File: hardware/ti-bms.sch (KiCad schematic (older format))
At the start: 43 parts, among them J1 Conn_02x04_Odd_Even, J2 Conn_02x03_Odd_Even, J4 CAN_TERM, U1 Pico, U2 MCP2515-xST, U3 SN65HVD230, U4 TPS62160DGK, U5 MAX3485, U6 MAX3485

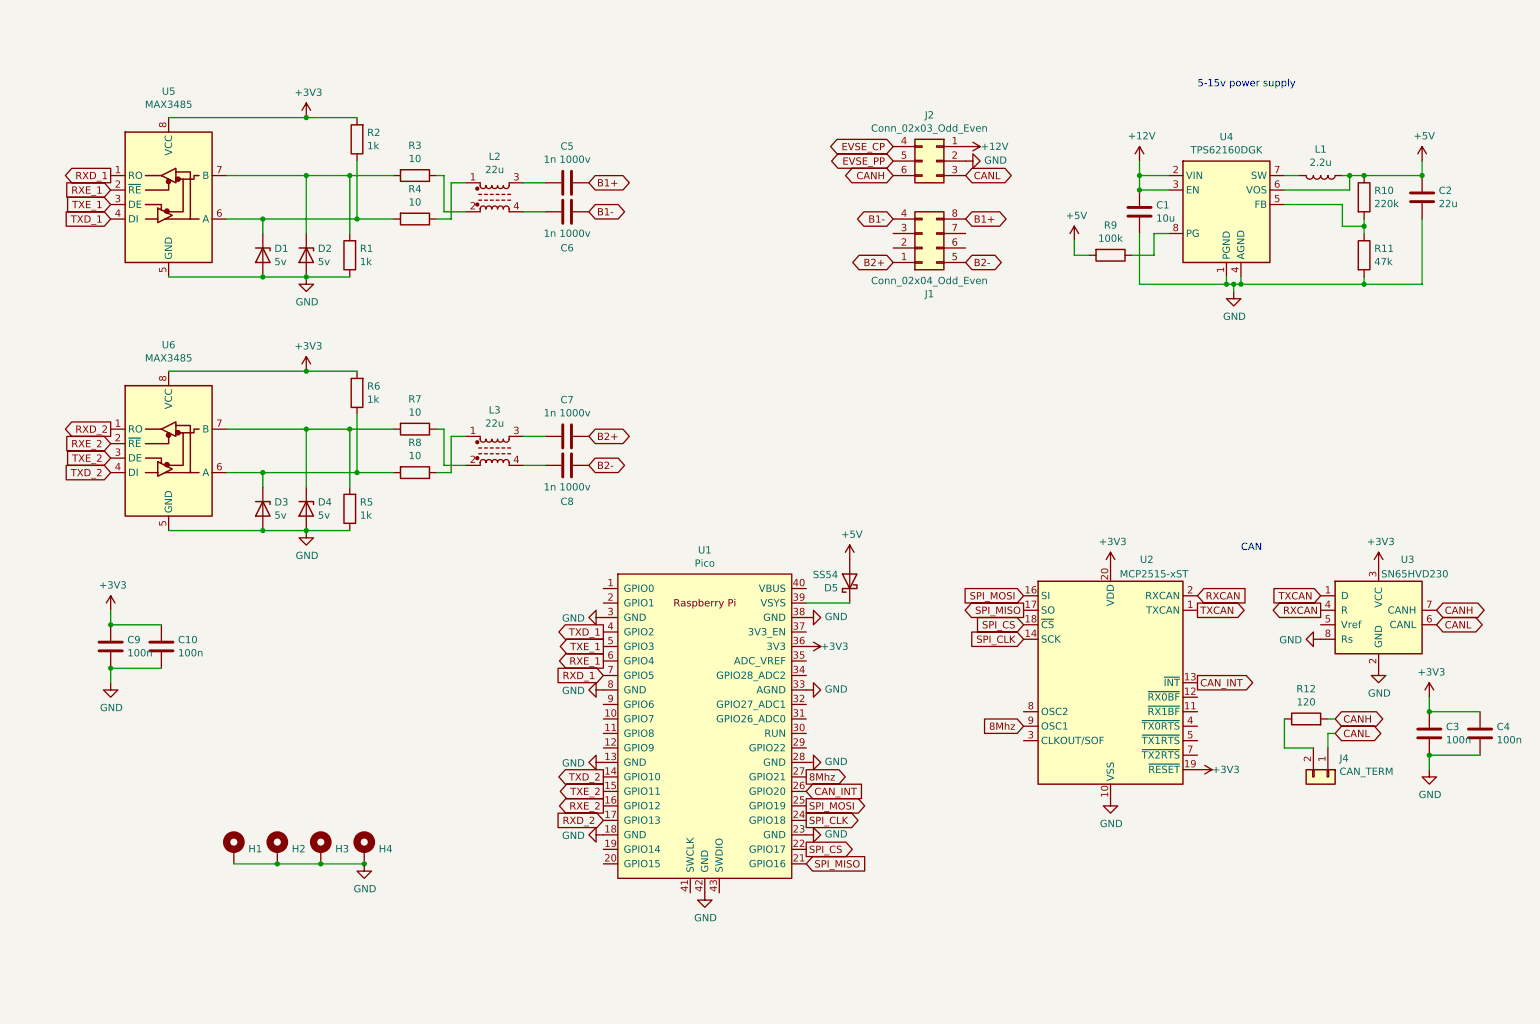
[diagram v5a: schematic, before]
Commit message: add 12v input and output, connect CAN line driver sleep pin
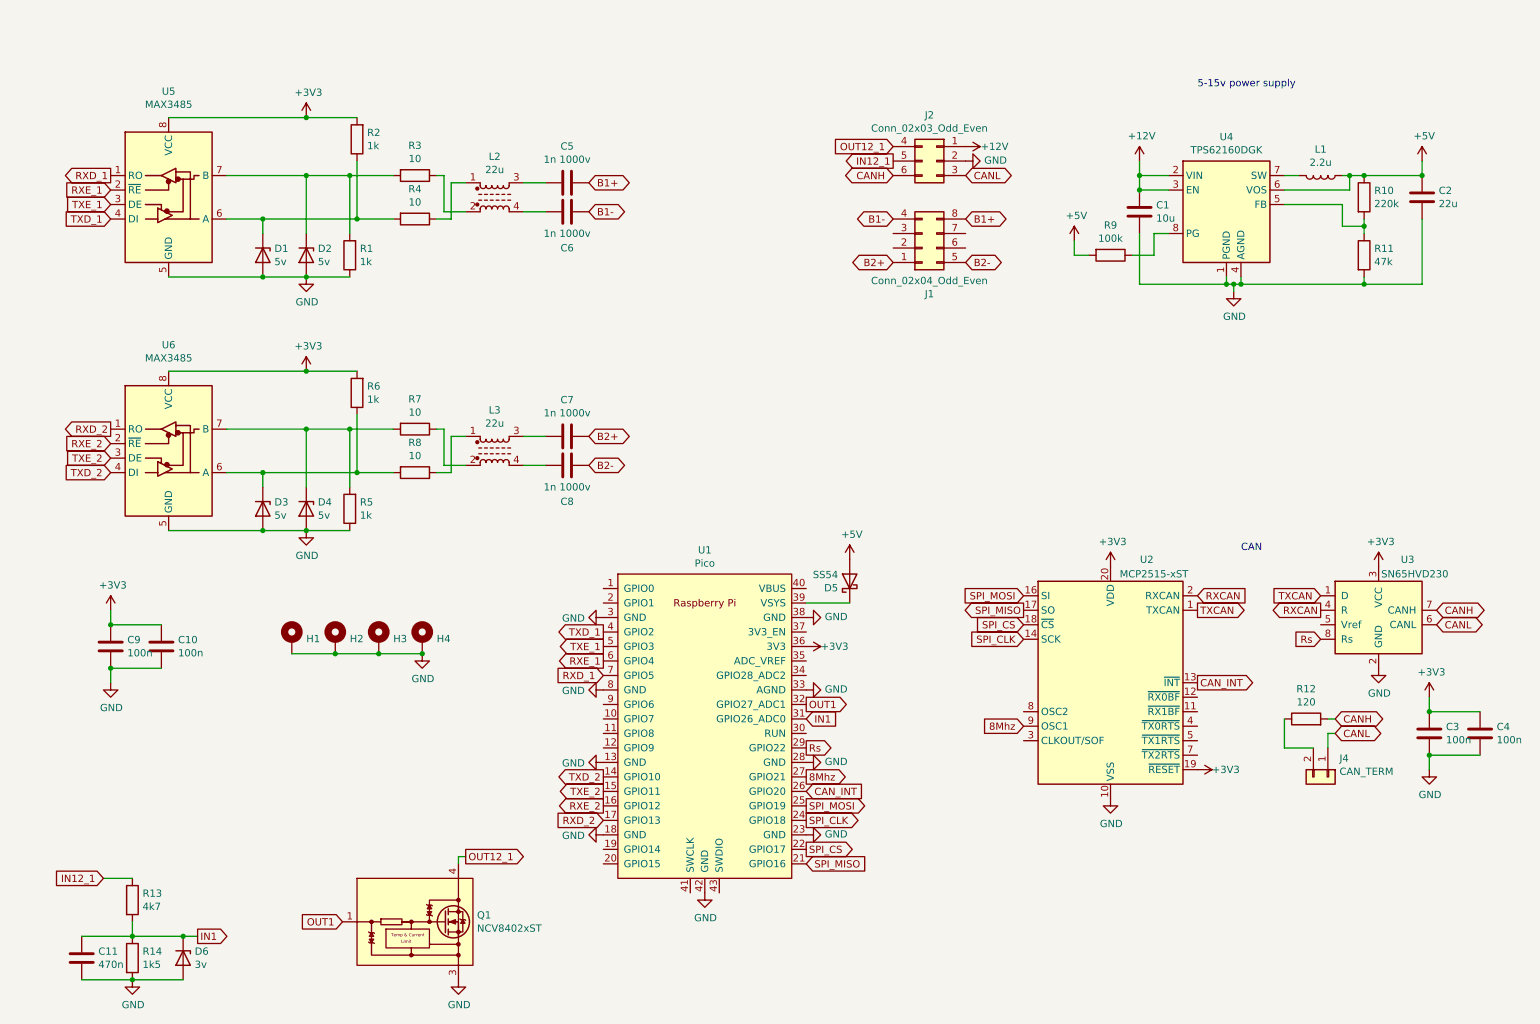
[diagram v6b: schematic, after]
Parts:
- added C11: 470n, Capacitor_SMD:C_0603_1608Metric, symbol Device:C
- added D6: 3v, Diode_SMD:D_MiniMELF, symbol Device:D_Zener
- added Q1: NCV8402xST, Package_TO_SOT_SMD:SOT-223, symbol Driver_FET:NCV8402xST
- added R13: 4k7, Resistor_SMD:R_0603_1608Metric, symbol Device:R
- added R14: 1k5, Resistor_SMD:R_0603_1608Metric, symbol Device:R
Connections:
- net GND: now also C11.2, D6.2 (A), Q1.3 (S), R14.2; no longer U3.8 (Rs)
- net Rs: now reaches U1.29 (GPIO22)
- net Rs: now also U3.8 (Rs)
- net IN1: now reaches U1.31 (GPIO26_ADC0)
- net IN1: now also C11.1, D6.1 (K), R13.2, R14.1
- net OUT1: now reaches U1.32 (GPIO27_ADC1)
- net OUT1: now also Q1.1 (G)
- net EVSE_CP renamed OUT12_1
- net OUT12_1: now also Q1.2 (D), Q1.4 (D)
- net EVSE_PP renamed IN12_1
- net IN12_1: now also R13.1
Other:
- moved on the sheet: H1, H2, H3, H4
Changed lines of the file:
@@
-$EndComp
-$Comp
-L power:GND #PWR024
-U 1 1 617A7038
-P 9650 4900
-F 0 "#PWR024" H 9650 4650 50  0001 C CNN
-F 1 "GND" V 9655 4772 50  0000 R CNN
-F 2 "" H 9650 4900 50  0001 C CNN
-F 3 "" H 9650 4900 50  0001 C CNN
-	1    9650 4900
-	0    1    1    0
 $EndComp
 $Comp
@@
 L Mechanical:MountingHole_Pad H1
 U 1 1 6199AFD3
-P 2150 6350
-F 0 "H1" H 2250 6353 50  0000 L CNN
-F 1 "MountingHole" H 2250 6308 50  0001 L CNN
-F 2 "MountingHole:MountingHole_3.2mm_M3_Pad" H 2150 6350 50  0001 C CNN
-F 3 "~" H 2150 6350 50  0001 C CNN
-	1    2150 6350
+P 2550 4900
+F 0 "H1" H 2650 4903 50  0000 L CNN
+F 1 "MountingHole" H 2650 4858 50  0001 L CNN
+F 2 "MountingHole:MountingHole_3.2mm_M3_Pad" H 2550 4900 50  0001 C CNN
+F 3 "~" H 2550 4900 50  0001 C CNN
+	1    2550 4900
 	1    0    0    -1
 $EndComp
@@
 L Mechanical:MountingHole_Pad H2
 U 1 1 6199C740
-P 2450 6350
-F 0 "H2" H 2550 6353 50  0000 L CNN
-F 1 "MountingHole" H 2550 6308 50  0001 L CNN
-F 2 "MountingHole:MountingHole_3.2mm_M3_Pad" H 2450 6350 50  0001 C CNN
-F 3 "~" H 2450 6350 50  0001 C CNN
-	1    2450 6350
+P 2850 4900
+F 0 "H2" H 2950 4903 50  0000 L CNN
+F 1 "MountingHole" H 2950 4858 50  0001 L CNN
+F 2 "MountingHole:MountingHole_3.2mm_M3_Pad" H 2850 4900 50  0001 C CNN
+F 3 "~" H 2850 4900 50  0001 C CNN
+	1    2850 4900
 	1    0    0    -1
 $EndComp
@@
 L Mechanical:MountingHole_Pad H3
 U 1 1 6199C8D6
-P 2750 6350
-F 0 "H3" H 2850 6353 50  0000 L CNN
-F 1 "MountingHole" H 2850 6305 50  0001 L CNN
-F 2 "MountingHole:MountingHole_3.2mm_M3_Pad" H 2750 6350 50  0001 C CNN
-F 3 "~" H 2750 6350 50  0001 C CNN
-	1    2750 6350
+P 3150 4900
+F 0 "H3" H 3250 4903 50  0000 L CNN
+F 1 "MountingHole" H 3250 4855 50  0001 L CNN
+F 2 "MountingHole:MountingHole_3.2mm_M3_Pad" H 3150 4900 50  0001 C CNN
+F 3 "~" H 3150 4900 50  0001 C CNN
+	1    3150 4900
 	1    0    0    -1
 $EndComp
@@
 L Mechanical:MountingHole_Pad H4
 U 1 1 6199CA74
-P 3050 6350
-F 0 "H4" H 3150 6353 50  0000 L CNN
-F 1 "MountingHole" H 3150 6305 50  0001 L CNN
-F 2 "MountingHole:MountingHole_3.2mm_M3_Pad" H 3050 6350 50  0001 C CNN
-F 3 "~" H 3050 6350 50  0001 C CNN
-	1    3050 6350
-	1    0    0    -1
-$EndComp
-Wire Wire Line
-	2150 6450 2450 6450
-Connection ~ 2450 6450
-Wire Wire Line
-	2450 6450 2750 6450
-Connection ~ 2750 6450
-Wire Wire Line
-	2750 6450 3050 6450
+P 3450 4900
+F 0 "H4" H 3550 4903 50  0000 L CNN
+F 1 "MountingHole" H 3550 4855 50  0001 L CNN
+F 2 "MountingHole:MountingHole_3.2mm_M3_Pad" H 3450 4900 50  0001 C CNN
+F 3 "~" H 3450 4900 50  0001 C CNN
+	1    3450 4900
+	1    0    0    -1
+$EndComp
+Wire Wire Line
+	2550 5000 2850 5000
+Connection ~ 2850 5000
+Wire Wire Line
+	2850 5000 3150 5000
+Connection ~ 3150 5000
+Wire Wire Line
+	3150 5000 3450 5000
 $Comp
 L power:GND #PWR031
 U 1 1 619B5460
-P 3050 6450
-F 0 "#PWR031" H 3050 6200 50  0001 C CNN
-F 1 "GND" H 3055 6277 50  0000 C CNN
-F 2 "" H 3050 6450 50  0001 C CNN
-F 3 "" H 3050 6450 50  0001 C CNN
-	1    3050 6450
-	1    0    0    -1
-$EndComp
-Connection ~ 3050 6450
+P 3450 5000
+F 0 "#PWR031" H 3450 4750 50  0001 C CNN
+F 1 "GND" H 3455 4827 50  0000 C CNN
+F 2 "" H 3450 5000 50  0001 C CNN
+F 3 "" H 3450 5000 50  0001 C CNN
+	1    3450 5000
+	1    0    0    -1
+$EndComp
+Connection ~ 3450 5000
 $Comp
 L Regulator_Switching:TPS62160DGK U4
@@
 	0    1    1    0
 $EndComp
-Text GLabel 6700 1500 0    50   BiDi ~ 0
-EVSE_CP
-Text GLabel 6700 1600 0    50   BiDi ~ 0
-EVSE_PP
 Text GLabel 7200 1700 2    50   BiDi ~ 0
 CANL
@@
 Wire Wire Line
 	1300 5100 1300 5200
+$Comp
+L Device:R R13
+U 1 1 61DD7F66
+P 1450 6700
+F 0 "R13" H 1520 6746 50  0000 L CNN
+F 1 "4k7" H 1520 6655 50  0000 L CNN
+F 2 "Resistor_SMD:R_0603_1608Metric" V 1380 6700 50  0001 C CNN
+F 3 "~" H 1450 6700 50  0001 C CNN
+F 4 "C23162" H 1450 6700 50  0001 C CNN "LCSC"
+	1    1450 6700
+	1    0    0    -1
+$EndComp
+$Comp
+L Device:R R14
+U 1 1 61DD8D2C
+P 1450 7100
+F 0 "R14" H 1520 7146 50  0000 L CNN
+F 1 "1k5" H 1520 7055 50  0000 L CNN
+F 2 "Resistor_SMD:R_0603_1608Metric" V 1380 7100 50  0001 C CNN
+F 3 "~" H 1450 7100 50  0001 C CNN
+F 4 "C22843" H 1450 7100 50  0001 C CNN "LCSC"
+	1    1450 7100
+	1    0    0    -1
+$EndComp
+$Comp
+L Device:D_Zener D6
+U 1 1 61DD9637
+P 1800 7100
+F 0 "D6" V 1754 7180 50  0000 L CNN
+F 1 "3v" V 1845 7180 50  0000 L CNN
+F 2 "Diode_SMD:D_MiniMELF" H 1800 7100 50  0001 C CNN
+F 3 "~" H 1800 7100 50  0001 C CNN
+F 4 "C8056" V 1800 7100 50  0001 C CNN "LCSC"
+	1    1800 7100
+	0    1    1    0
+$EndComp
+$Comp
+L Device:C C11
+U 1 1 61DD9B38
+P 1100 7100
+F 0 "C11" H 1215 7146 50  0000 L CNN
+F 1 "470n" H 1215 7055 50  0000 L CNN
+F 2 "Capacitor_SMD:C_0603_1608Metric" H 1138 6950 50  0001 C CNN
+F 3 "~" H 1100 7100 50  0001 C CNN
+F 4 "C1623" H 1100 7100 50  0001 C CNN "LCSC"
+	1    1100 7100
+	1    0    0    -1
+$EndComp
+$Comp
+L Driver_FET:NCV8402xST Q1
+U 1 1 61DDABE2
+P 3400 6850
+F 0 "Q1" H 3828 6896 50  0000 L CNN
+F 1 "NCV8402xST" H 3828 6805 50  0000 L CNN
+F 2 "Package_TO_SOT_SMD:SOT-223" H 3400 6570 50  0001 C CNN
+F 3 "https://www.onsemi.com/pub/Collateral/NCV8402-D.PDF" H 3700 6850 50  0001 C CNN
+F 4 "C77755" H 3400 6850 50  0001 C CNN "LCSC"
+	1    3400 6850
+	1    0    0    -1
+$EndComp
+Text GLabel 2900 6850 0    50   Input ~ 0
+OUT1
+Text GLabel 3750 6400 2    50   Output ~ 0
+OUT12_1
+Wire Wire Line
+	3750 6400 3700 6400
+Wire Wire Line
+	3700 6400 3700 6450
+Wire Wire Line
+	1450 6850 1450 6950
+Wire Wire Line
+	1100 6950 1450 6950
+Connection ~ 1450 6950
+Wire Wire Line
+	1100 7250 1450 7250
+Wire Wire Line
+	1450 7250 1800 7250
+Connection ~ 1450 7250
+Wire Wire Line
+	1800 6950 1450 6950
+$Comp
+L power:GND #PWR0108
+U 1 1 61DBD09A
+P 1450 7250
+F 0 "#PWR0108" H 1450 7000 50  0001 C CNN
+F 1 "GND" H 1455 7077 50  0000 C CNN
+F 2 "" H 1450 7250 50  0001 C CNN
+F 3 "" H 1450 7250 50  0001 C CNN
+	1    1450 7250
+	1    0    0    -1
+$EndComp
+$Comp
+L power:GND #PWR0109
+U 1 1 61DBD4E0
+P 3700 7250
+F 0 "#PWR0109" H 3700 7000 50  0001 C CNN
+F 1 "GND" H 3705 7077 50  0000 C CNN
+F 2 "" H 3700 7250 50  0001 C CNN
+F 3 "" H 3700 7250 50  0001 C CNN
+	1    3700 7250
+	1    0    0    -1
+$EndComp
+Text GLabel 1900 6950 2    50   Output ~ 0
+IN1
+Text GLabel 1250 6550 0    50   Input ~ 0
+IN12_1
+Wire Wire Line
+	1250 6550 1450 6550
+Wire Wire Line
+	1800 6950 1900 6950
+Connection ~ 1800 6950
+Text GLabel 6100 5450 2    50   Input ~ 0
+IN1
+Text GLabel 6100 5350 2    50   Output ~ 0
+OUT1
+Text GLabel 6700 1500 0    50   Input ~ 0
+OUT12_1
+Text GLabel 6700 1600 0    50   Output ~ 0
+IN12_1
+Text GLabel 9650 4900 0    50   Input ~ 0
+Rs
+Text GLabel 6100 5650 2    50   Output ~ 0
+Rs
 $EndSCHEMATC

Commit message: v3
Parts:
- removed J1: Conn_02x04_Odd_Even, Connector_Molex:Molex_Micro-Fit_3.0_43045-0800_2x04_P3.00mm_Horizontal, symbol Connector_Generic:Conn_02x04_Top_Bottom
- added C12, C13: 1n 1000v, Capacitor_SMD:C_1206_3216Metric, symbol Device:C
- added C14: 100n, Capacitor_SMD:C_0603_1608Metric, symbol Device:C
- added D7, D8: 5v, footprints:SOD882, symbol Device:D_Zener
- added J2, J3, J4: Conn_01x02, Connector_Molex:Molex_Micro-Fit_3.0_43650-0200_1x02_P3.00mm_Horizontal, symbol Connector_Generic:Conn_01x02
- added L4: 22u, footprints:ACT45B-101-2P-TL003, symbol Device:L_Core_Ferrite_Coupled_1324
- added R15, R16: 1k, Resistor_SMD:R_0603_1608Metric, symbol Device:R
- added R17, R18: 10, Resistor_SMD:R_0603_1608Metric, symbol Device:R
- added U7: MAX3485, Package_SO:SOP-8_3.9x4.9mm_P1.27mm, symbol Interface_UART:MAX3485
- renumbered J2 to J1, J4 to J5
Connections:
- net +3V3: now also C14.1, R16.2, U7.8 (VCC)
- net B1+: now also C6.1, J2.2 (Pin_2); no longer C5.1
- net B1-: now also C5.1, J2.1 (Pin_1); no longer C6.1
- net B2+: now also C8.1, J3.2 (Pin_2); no longer C7.1
- net B2-: now also C7.1, J3.1 (Pin_1); no longer C8.1
- net GND: now also C14.2, D7.2 (A), D8.2 (A), R15.1, U7.5 (GND)
- net RXD_2: now also U1.12 (GPIO9); no longer U1.17 (GPIO13)
- net RXE_2: now also U1.11 (GPIO8); no longer U1.16 (GPIO12)
- net TXD_2: now also U1.9 (GPIO6); no longer U1.14 (GPIO10)
- net TXE_2: now also U1.10 (GPIO7); no longer U1.15 (GPIO11)
- net at L2.3: now also C6.2; no longer C5.2
- net at L2.4: now also C5.2; no longer C6.2
- net at L3.3: now also C8.2; no longer C7.2
- net at L3.4: now also C7.2; no longer C8.2
- new net: D7.1 (K), R16.1, R18.2, U7.6 (A)
- new net: D8.1 (K), R15.2, R17.2, U7.7 (B)
- new net: L4.2, R17.1
- new net: L4.1, R18.1
- new net: C13.2, L4.3
- new net: C12.2, L4.4
- new net B3+: C13.1, J4.2 (Pin_2)
- new net B3-: C12.1, J4.1 (Pin_1)
- new net RXD_3: U1.17 (GPIO13), U7.1 (RO)
- new net RXE_3: U1.16 (GPIO12), U7.2 (~RE)
- new net TXD_3: U1.14 (GPIO10), U7.4 (DI)
- new net TXE_3: U1.15 (GPIO11), U7.3 (DE)
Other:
- note removed: "5-15v power supply"
- moved on the sheet: C1, C10, C2, C5, C6, C7, C8, C9, D1, D2, D3, D4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
